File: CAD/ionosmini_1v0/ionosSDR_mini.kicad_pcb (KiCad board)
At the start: 4 copper layers, 168 x 80 mm, 63 parts, among them CON1 TFC-120-02-F-D-A-K-TR, CON2 TFC-120-02-F-D-A-K-TR, IC1 ESP32-S3-DEVKITC-1-N8R2, SW1 PTS647SK38SMTR2 LFS, SW2 PTS647SK38SMTR2 LFS, SW3 PTS647SK38SMTR2 LFS, SW4 PTS647SK38SMTR2 LFS, SW5 BACK, SW6 OK, U1 LP5907MFX-3.3

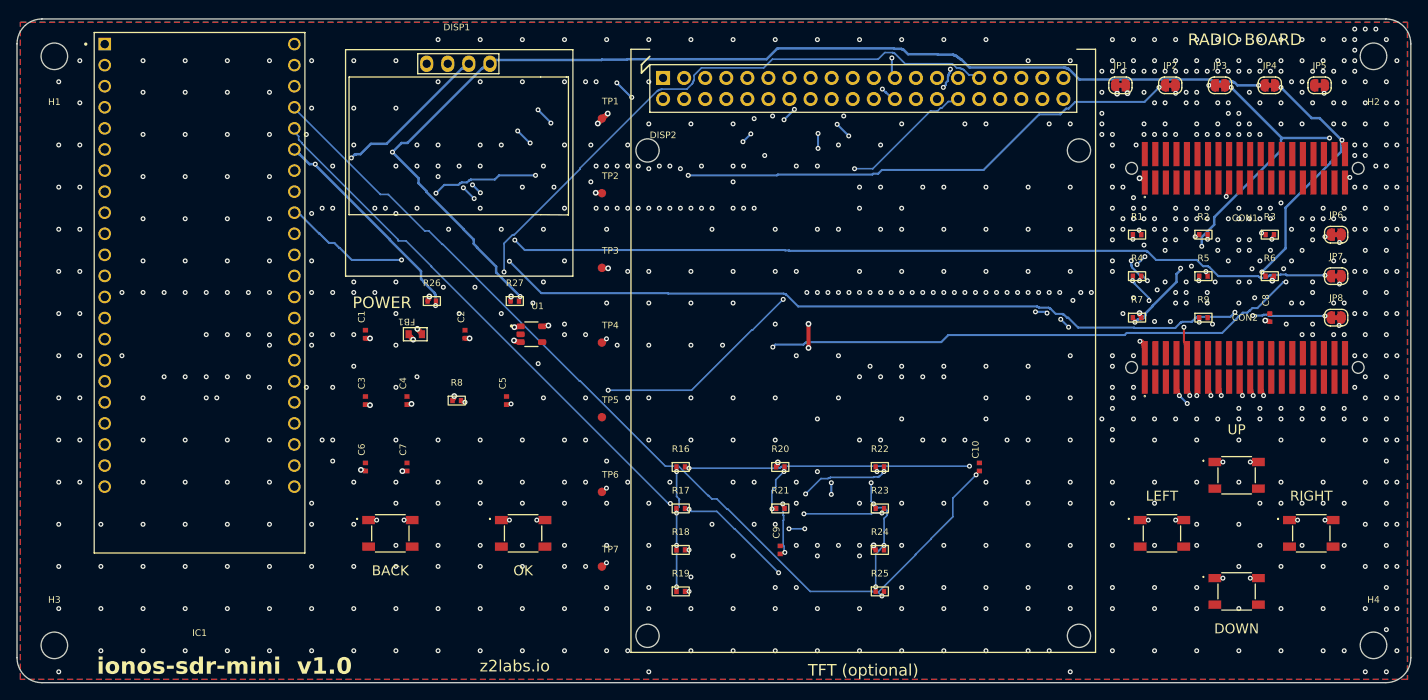
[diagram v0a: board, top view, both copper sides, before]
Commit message: rev-B3-2L: 2-layer variant, full re-route on both layers
Same placement as rev-B3, JLC 2-layer FR-4 1.6 mm (F.Cu 35 um | core
1.53 mm | B.Cu 35 um, er 4.5 assumed - JLC publishes none). No plane: GND
pour and tracks on both layers, every track is a microstrip over the GND
pour of the other layer (~128 ohm at 0.25 mm).

Routing: power -> fast nets -> rest, earlier copper fixed. B.Cu is open
but costs extra (2 / 3 / 1.5) so it carries crossings and the F.Cu tracks
keep a GND return path under them; via cost 5000 um. Four variants were
compared (B.Cu cost and via cost); this one keeps the best return path for
the fast nets: 74.3 % of their length has GND right under it on the other
layer, 186 routing vias, 4604 mm, 98 % on the 45 deg grid.
F.Cu 3625 mm, B.Cu 979 mm. B.Cu GND pour is one piece.

GND stitching to the fixed point (532 vias, 6 rounds), one more via for an
orphaned F.Cu island at C2.2: 719 vias in total.

DRC 0/0/0 with schematic parity.
Twin (spec only, the code stays general): 2-layer STACKUP marked as
assumed, LINE_LAYERS = F.Cu / B.Cu microstrip, series-R candidates up to
82 ohm. L1 66/6/0, L2 70/1/0, L3 28/3/0, L4 15/3/0, L5 15/4/2 (non-keyed
connector STEP). Z0 127.8 ohm (twin) vs 128.1 ohm (2-D Laplace).
On two layers R1-R5 must be fitted: 0 ohm gives 30-41 % VDD overshoot on
the FG23 bus, 68 ohm 0.4-2.7 %. CON1/CON2 orientation references
re-captured (diff: new top tracks, vias, TFT edge; bodies unchanged),
self-test 2/2.
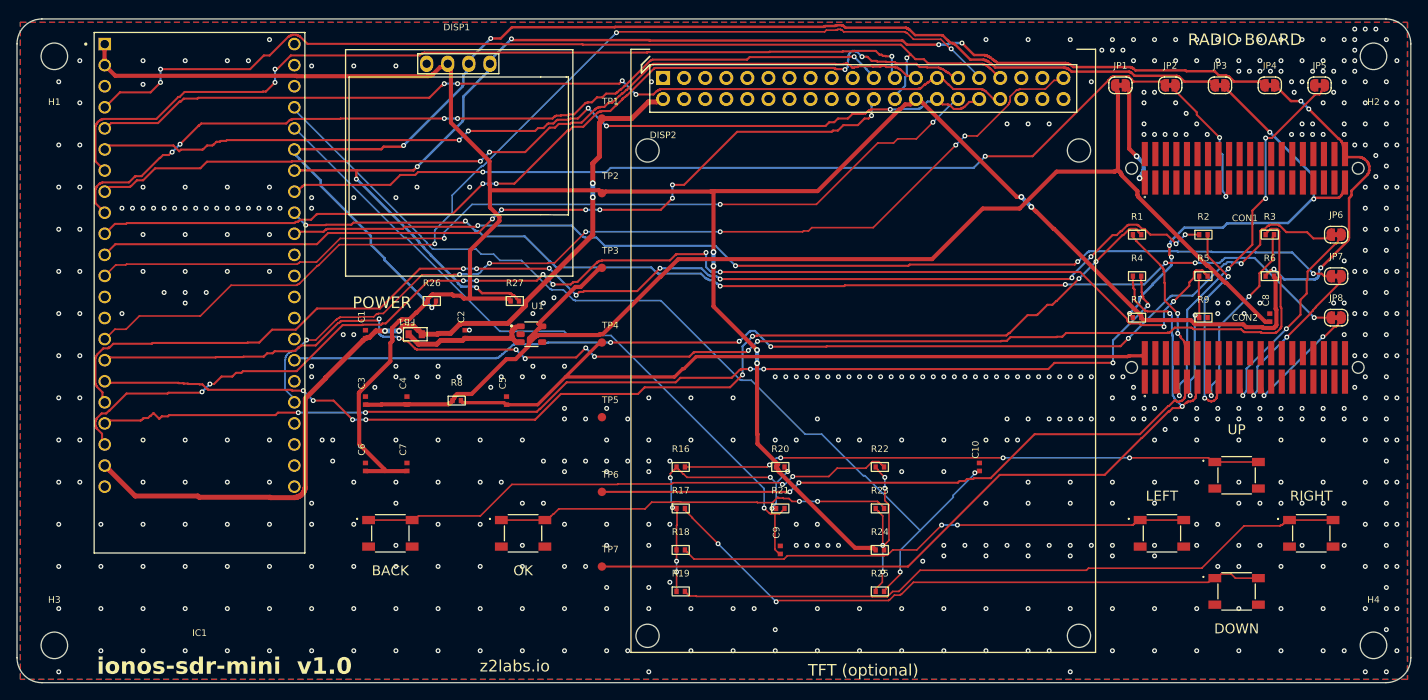
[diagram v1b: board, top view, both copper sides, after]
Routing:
- net 3V3: track 310.3 -> 289.1 mm, vias 11 -> 6
- net 3V3_RADIO: track 171.1 -> 153.1 mm, vias 7 -> 0
- net FG23_CS: track 146.6 -> 163.7 mm, vias 5 -> 8
- net FG23_SCLK: track 140.8 -> 150.9 mm, vias 1 -> 10
- net Net-(IC1-GPIO14): track 147.6 -> 156.6 mm, vias 3 -> 10
- net I2C_SDA_RB: track 33.0 -> 39.4 mm, vias 3 -> 4
- net I2C_SDA: track 149.1 -> 155.2 mm, vias 3 -> 6
- net TFT_CS: track 103.6 -> 109.6 mm, vias 1 -> 3
- net I2C_SCL: track 142.4 -> 148.2 mm, vias 4 -> 3
- net 5V0: track 98.6 -> 103.9 mm
- net FG23_MOSI: track 133.4 -> 138.7 mm, vias 1 -> 8
- net TCH_INT: track 109.2 -> 114.1 mm, vias 2 -> 7
- net TFT_SCK: track 115.9 -> 120.8 mm, vias 5 -> 3
- net Net-(IC1-GPIO13): track 133.2 -> 137.6 mm, vias 1 -> 6
- net TFT_RST: track 100.8 -> 105.0 mm, vias 6 -> 5
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- removed copper zone on In1.Cu, net GND
- removed copper zone on In2.Cu, net GND
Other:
- copper layers 4 -> 2

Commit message: rev-B3-2L PCB: pin map v2 parts, full re-route with 0/45/90 deg tracks
New parts placed as on the 4-layer board: C11/C12 at the TFT VDD pin,
R28-R32 header pull-ups under the display socket, R33 (NA 0R) and TP8
next to the radio board sockets, R34 and the optional SW7 SPARE key.

All tracks and vias ripped and re-routed in three passes (power, the
FG23 / TFT buses, the rest), B.Cu open at a cost so it carries short
crossings and the GND return pour stays mostly whole. Octilinear only:
0 % any-angle segments, staircases straightened (1259 -> 1067
segments), then GND stitching on the new geometry (844 vias).

Design rules: the generic 0.10 mm clearance rule also set the zone
filler's clearance, so the GND pour came 0.10 mm from every pad and the
DevKit header pads' 0.10 mm mask expansion bridged onto it (70
solder_mask_bridge). A pour rule at the end of the .kicad_dru keeps
pours 0.3 mm from other nets.

Silkscreen to JLCPCB rules; references that sat on pads or on another
part's silk moved, FB1 turned upright, TP8 label pulled in from the
board edge. lib_footprint_mismatch warnings are expected: the board
copies of those footprints carry the trimmed silk.

TFC-120-02-F-D-A STEP replaced with the current Samtec model; twin 3D
reference images recaptured, key still at the pin 1 end. DISP1 3D
offset corrected; twin_3d registers each model's pins against its pads.

DRC 0 errors, 0 unconnected, schematic parity 0. twin_analog on this
routing recommends R1-R5 = 82 ohm (README updated; 22 ohm stays on the
4-layer board). README: buttons and ladders, VRF_IN / 5V_RADIO, display
and touch section, DevKit clone vs official board note, new 3D render.
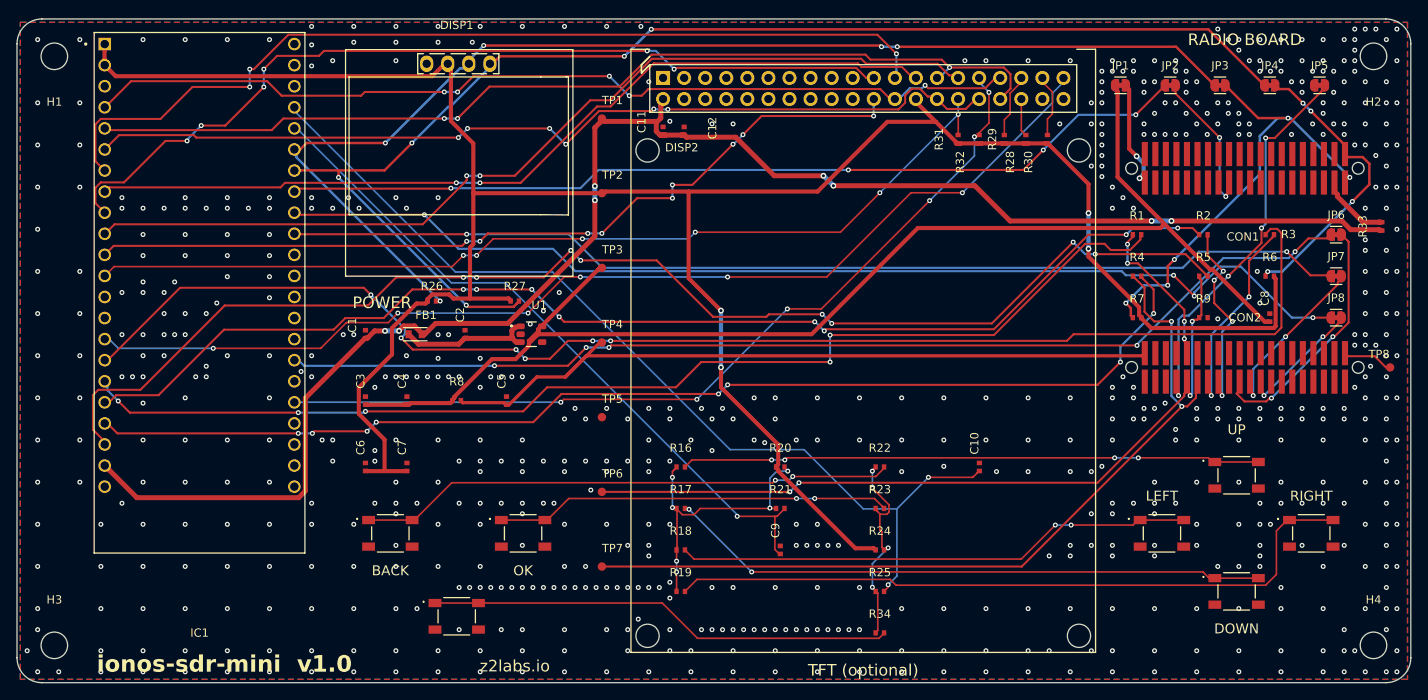
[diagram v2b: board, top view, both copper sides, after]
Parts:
- added C11: 10uF/6.3V, rpw_lib:CAPC1005X60_0402, F.Cu at (127.9, 63.5)
- added C12: 100nF/50V/10%, rpw_lib:CAPC1005X60_0402, F.Cu at (130.4, 63.5)
- added R28: 10k, rpw_lib:RESC1005X40_0402, F.Cu at (169.0, 64.5)
- added R29: 10k, rpw_lib:RESC1005X40_0402, F.Cu at (171.6, 64.5)
- added R30: 10k, rpw_lib:RESC1005X40_0402, F.Cu at (174.2, 64.5)
- added R31: 4.7k, rpw_lib:RESC1005X40_0402, F.Cu at (163.4, 64.5)
- added R32: 4.7k, rpw_lib:RESC1005X40_0402, F.Cu at (166.0, 64.5)
- added R33: NA(0R), rpw_lib:RESC1005X40_0402, F.Cu at (214.5, 75.0)
- added R34: 6.8k/1%, rpw_lib:RESC1005X40_0402, F.Cu at (154.0, 124.0)
- added SW7: NA(PTS647SK38), rpw_lib:PTS647SK38SMTR2LFS, F.Cu at (103.0, 122.0)
- added TP8: VRF_IN, rpw_lib:TESTPOINT_40MIL_SMD, F.Cu at (215.5, 92.0)
- C1, C6: value 10u -> 10uF/6.3V
- C10, C4, C5, C7, C8, C9: value 100n -> 100nF/50V/10%
- C2, C3: value 1u -> 1uF/16V/10%
- JP1, JP2, JP3, JP4, JP5, JP6, JP7, JP8: value ~ -> Bridged
- R17, R23: value 2k2 -> 2.2k/1%
- R18: value 6k8 -> 6.8k/1%
- R19: value 22k -> 22k/1%
- R20, R24: value 10k -> 10k/1%
- R26, R27: value 4k7 DNP -> NA(4.7k)
- SW5: value BACK -> PTS647SK38SMTR2 LFS
- SW6: value OK -> PTS647SK38SMTR2 LFS
- U1: value LP5907MFX-3.3 -> LP5907MFX-3.3(SOT23-5)
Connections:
- CON1 pad 37: unconnected-(CON1-Pad37) -> 5V_RADIO
- CON2 pad 40: unconnected-(CON2-Pad40) -> VRF_IN
- DISP2 pad 35: unconnected-(DISP2-SD_/CS-Pad35) -> SD_CS
- DISP2 pad 36: unconnected-(DISP2-FONT_/CS-Pad36) -> FONT_CS
- DISP2 pad 37: unconnected-(DISP2-FLASH_/CS-Pad37) -> FLASH_CS
- IC1 pad J1_15: TCH_B -> TCH_INT
- IC1 pad J3_18: TCH_INT -> TCH_B
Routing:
- net 5V0: track 103.9 -> 199.2 mm, vias 4 -> 8
- net BTN_A3: track 0.00 -> 56.2 mm
- net TCH_B: track 125.5 -> 105.1 mm, vias 3 -> 6
- net TCH_INT: track 114.1 -> 130.5 mm, vias 7 -> 6
- net 5V_RADIO: track 0.00 -> 8.47 mm
- net 3V3: track 289.1 -> 297.0 mm, vias 6 -> 4
- net SD_CS: track 0.00 -> 7.73 mm
- net FLASH_CS: track 0.00 -> 7.63 mm
- net TFT_MOSI: track 112.7 -> 119.6 mm, vias 4 -> 3
- net TFT_SCK: track 120.8 -> 114.1 mm, vias 3 -> 5
- net VRF_IN: track 0.00 -> 6.16 mm
- net FG23_SCLK: track 150.9 -> 145.1 mm, vias 10 -> 8
- net FONT_CS: track 0.00 -> 4.57 mm
- net SWO_RB: track 26.1 -> 30.4 mm
- net I2C_SCL: track 148.2 -> 144.4 mm, vias 3 -> 5
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
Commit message: PCB: stitch every GND pour pocket, centre tracks in their channels
The zone filler drops pieces of GND pour that have no connection
(island removal), so a strip of GND between two tracks with no via in
it was simply missing - white holes all over the 2-layer F.Cu. Every
such pocket now gets a via into connected GND on another layer
(0.45/0.3 mm where the 0.6/0.3 via does not fit), and the next fill
keeps it. What is left is narrower than a via, or has no connected
GND on any other layer to tie to (e.g. between the TFT header rows).

Straight runs that pass between obstacles on both sides (a track
between two header pins) are moved to the middle of the channel; the
neighbouring segments stay on their own lines, so the routing stays
0/45/90 deg.

DRC 0 errors, 0 unconnected, schematic parity 0; twin unchanged.
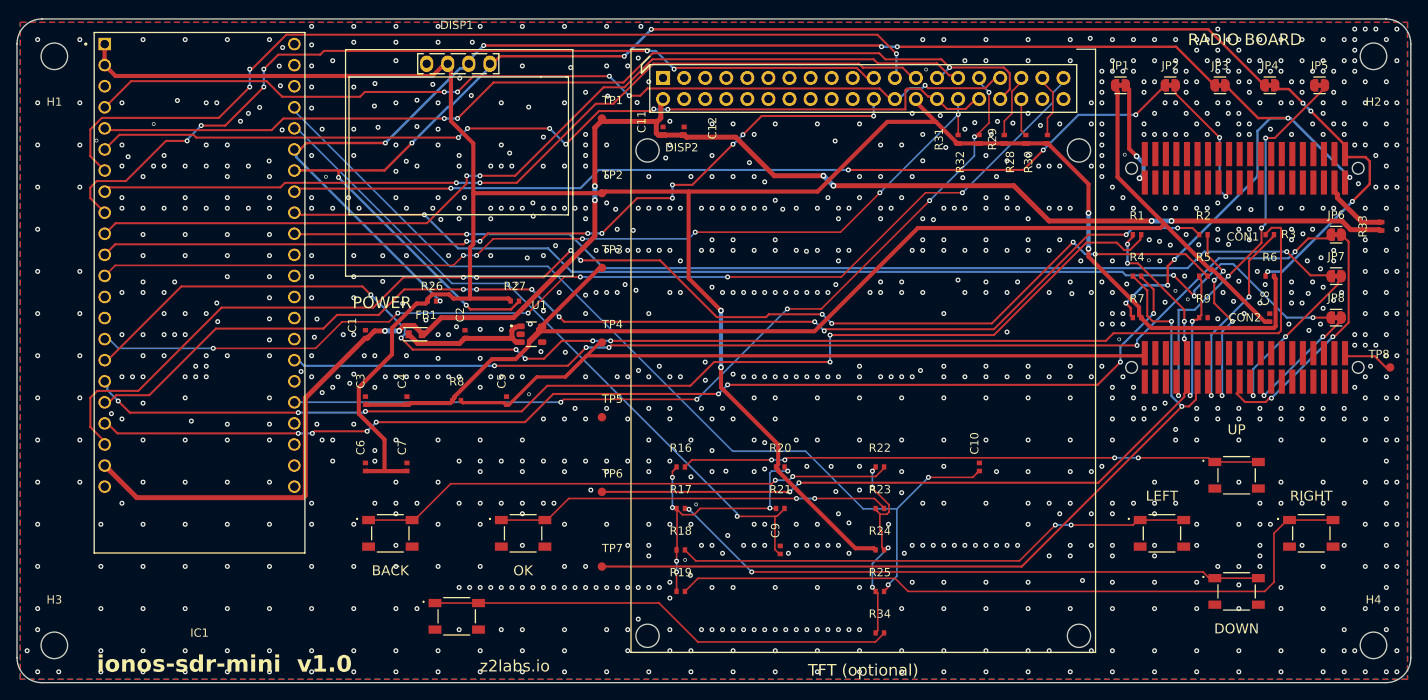
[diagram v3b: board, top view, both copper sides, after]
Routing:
- net BTN_B4: track 85.3 -> 86.4 mm
- net TFT_RST: track 106.9 -> 107.8 mm
- net TFT_MISO: track 112.3 -> 113.2 mm
- net FG23_CS: track 165.7 -> 166.4 mm
- net FG23_SPARE_RB: track 47.6 -> 48.3 mm
- net I2C_SCL_RB: track 55.5 -> 56.0 mm
- net TFT_CS: track 112.3 -> 112.8 mm
- net GND: vias 654 -> 1154

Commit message: SWD debug header CON3 (1x6 2.54 mm, not fitted) for an external debugger
Flashing the FG23 so far went only through the ESP32's bit-banged SWD.
CON3 adds a row of six plated holes on the right board edge, outside
the radio board's outline, for a J-Link / Simplicity Link with a pogo
clip or solder-in pins. Pin order follows the Tag-Connect TC2030-CTX:
1 VTref (VMCU_IN), 2 SWDIO, 3 nRESET, 4 SWCLK, 5 GND, 6 SWO.

The pins are on the radio side of the solder-jumper cut points
(SWDIO_RB, SWCLK_RB, SWO_RB, RESETn_RB): with JP2 and JP6-JP8 cut the
ESP32 is off the bus entirely; uncut, firmware keeps its SWD pins as
inputs while a debugger is attached. VTref only senses VMCU.

Schematic: radio sheet, new block with KiCad's TC2030 symbol (VCC top,
GND bottom) on a 1x6 header footprint; lint clean, ERC 0 errors.
twin_check asserts every CON3 pin reaches its radio-board pin.
twin_3d resolves KiCad's own ${KICADnn_3DMODEL_DIR} from the install.

PCB: TP8 moves 2 mm down to make room; full re-route (0/45/90). On two
layers the SWD nets are routed first (after the power pass RESETn_RB
had no way to the edge), and a net a pass cannot route is re-routed
together with its neighbours. The GND pads of C1 and R9 ended up
walled in by tracks; each got a GND via next to the pad and the nets in
the way were re-routed around it. GND pockets stitched, tracks centred
in their channels. DRC 0 errors, 0 unconnected, schematic parity 0.
3D reference images recaptured. README: SWD header section.
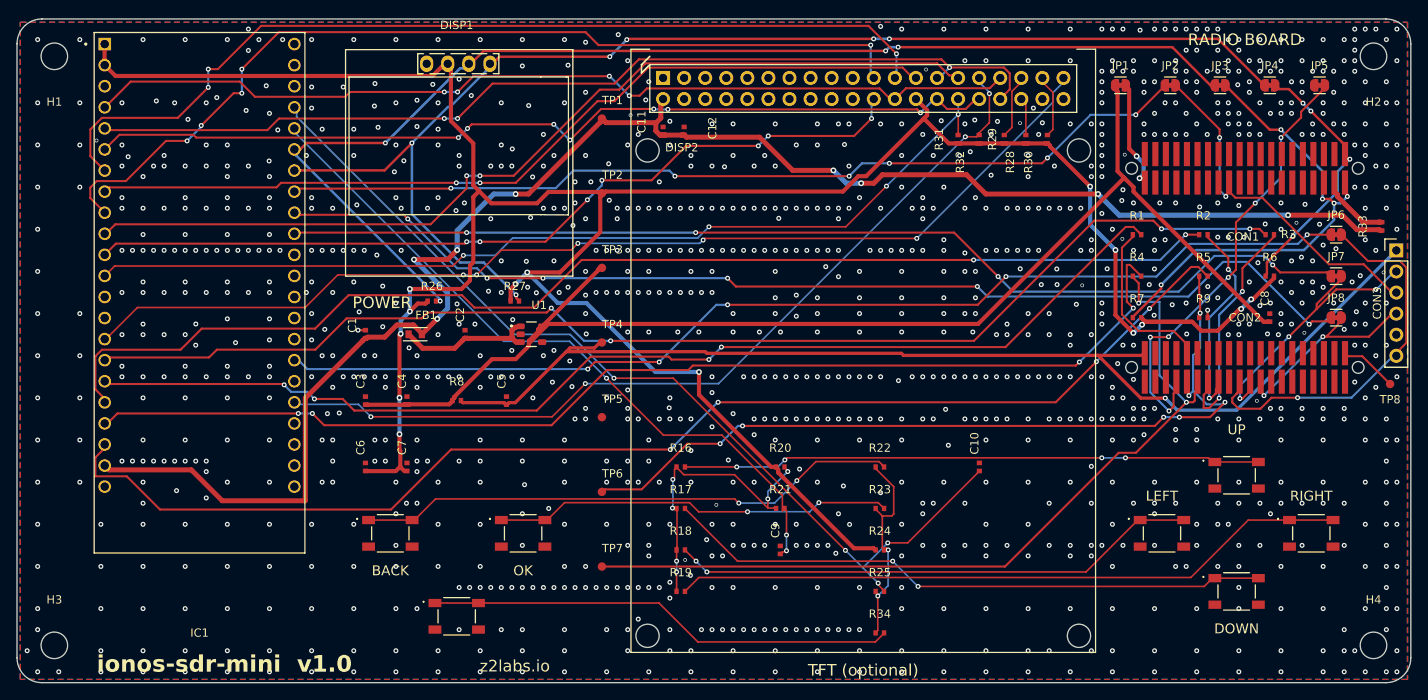
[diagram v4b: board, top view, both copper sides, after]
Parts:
- added CON3: NA(SWD 1x6 2.54), Connector_PinHeader_2.54mm:PinHeader_1x06_P2.54mm_Vertical, F.Cu at (216.2, 77.9)
- moved TP8 2.00 mm to (215.5, 94.0)
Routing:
- net VMCU_IN: track 91.3 -> 137.0 mm, vias 0 -> 1
- net RESETn_RB: track 17.8 -> 44.0 mm
- net 3V3: track 297.0 -> 320.7 mm, vias 4 -> 14
- net SWO_RB: track 30.4 -> 46.2 mm, vias 2 -> 1
- net FG23_CS: track 166.4 -> 150.9 mm, vias 6 -> 4
- net SWDIO_RB: track 20.6 -> 34.0 mm, vias 2 -> 3
- net SWCLK_RB: track 15.3 -> 25.0 mm
- net FG23_RDY: track 94.1 -> 101.6 mm, vias 4 -> 7
- net FG23_SPARE_RB: track 48.3 -> 54.1 mm, vias 4 -> 6
- net Net-(IC1B-GPIO14): track 158.1 -> 152.6 mm, vias 8 -> 4
- net BTN_B4: track 86.4 -> 81.7 mm
- net I2C_SDA: track 156.6 -> 152.1 mm, vias 5 -> 6
- net 5V0: track 199.7 -> 204.0 mm
- net TFT_RST: track 107.8 -> 112.1 mm, vias 6 -> 5
- net I2C_SDA_RB: track 35.9 -> 31.8 mm
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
